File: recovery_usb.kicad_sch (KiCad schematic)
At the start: 19 parts, among them J3 USB-C_WE_632723300011, U56 HD3SS3220IRNHR, U57 TPD4E05U06QDQARQ1, U58 TPD4E05U06QDQARQ1, U59 TPD4E05U06QDQARQ1

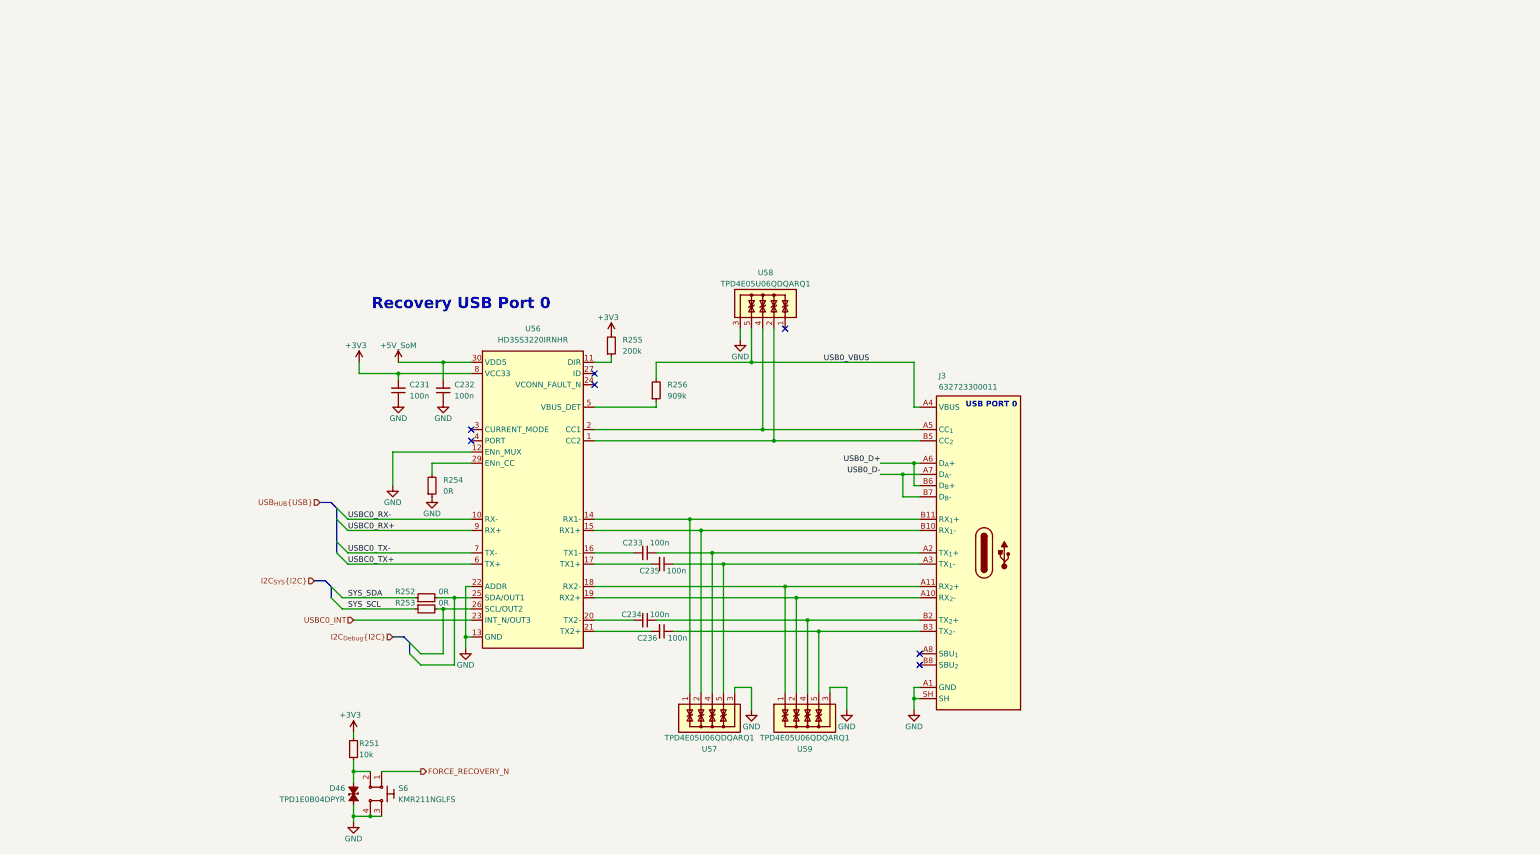
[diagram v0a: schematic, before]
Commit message: [#82837] Fix USB recovery and flashing section
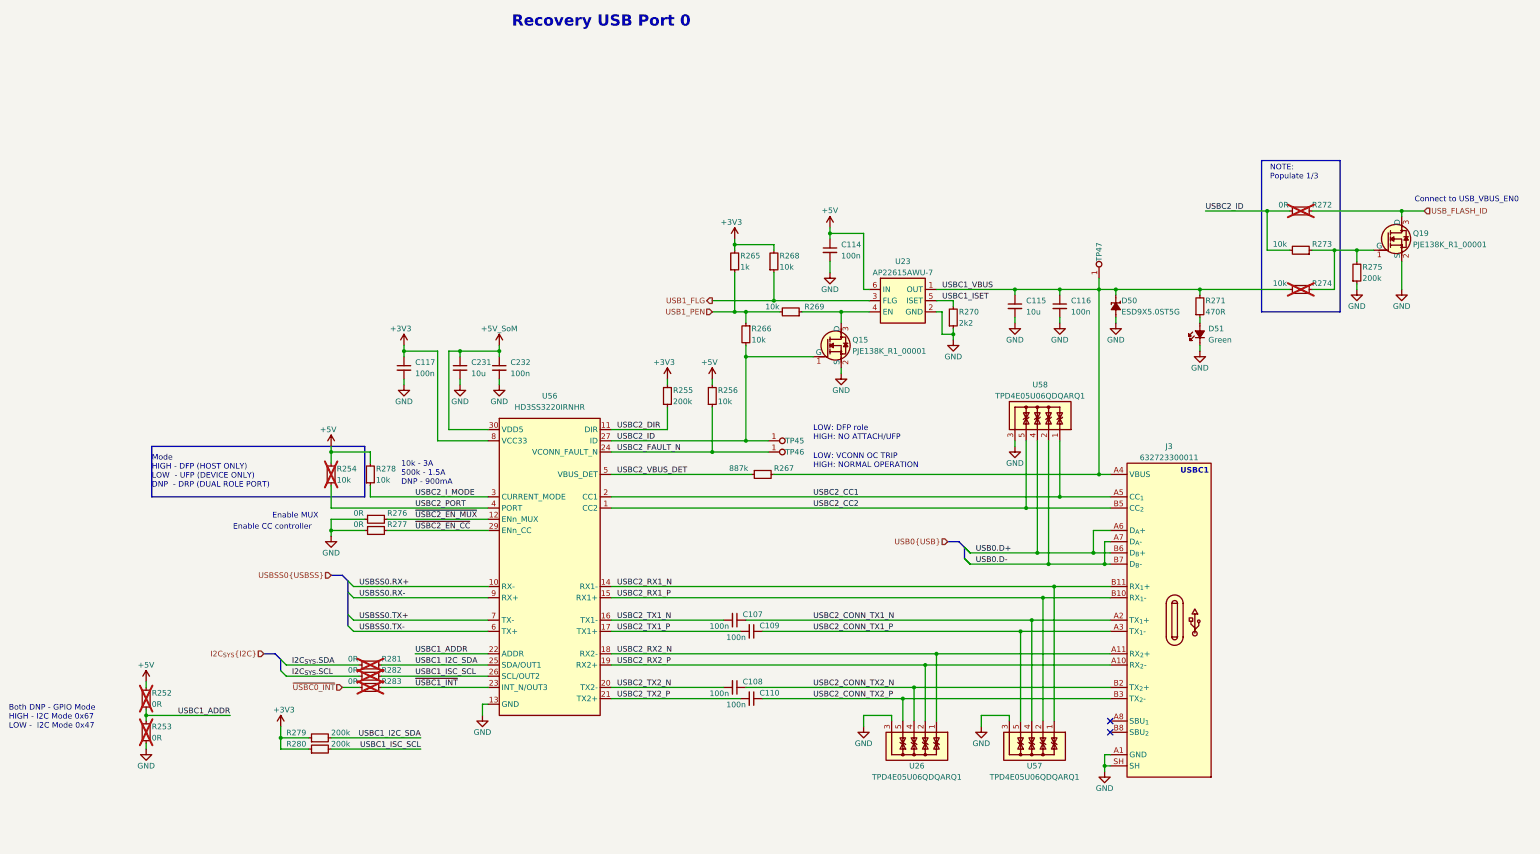
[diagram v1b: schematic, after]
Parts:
- removed C231, C232: C_100n_50V_X8L_0402, antmicro-footprints:C_0402_1005Metric, symbol antmicroCapacitors0402:C_100n_50V_X8L_0402
- removed C233, C234, C235, C236: C_100n_0201, antmicro-footprints:C_0201, symbol antmicroCapacitorsmisc:C_100n_0201
- removed D46: TPD1E0B04_XDFN-2, antmicro-footprints:XDFN-2_1x0.60mm, symbol antmicroTVSDiodes:TPD1E0B04_XDFN-2
- removed R251: R_10k_0402, antmicro-footprints:R_0402_1005Metric, symbol antmicroResistors0402:R_10k_0402
- removed R254: R_0R_0402, antmicro-footprints:R_0402_1005Metric, symbol antmicroResistors0402:R_0R_0402
- removed R256: R_909k_0402, antmicro-footprints:R_0402_1005Metric, symbol antmicroResistors0402:R_909k_0402
- removed S6: SW_KMR211NGLFS_SMD, antmicro-footprints:SW_KMR211NGLFS_SMD, symbol antmicroPushbuttonSwitches:SW_KMR211NGLFS_SMD
- removed U59: TPD4E05U06QDQARQ1, antmicro-footprints:USON-10_2.5x1mm_P0.5mm, symbol antmicroTVSDiodes:TPD4E05U06QDQARQ1
- added C107, C108, C109, C110, C114, C116, C117, C232: C_100n_0402, antmicro-footprints:C_0402_1005Metric, symbol antmicroCapacitors0402:C_100n_0402
- added C115, C231: C_10u_0603, antmicro-footprints:C_0603_1608Metric, symbol antmicroCapacitors0603:C_10u_0603
- added D50: ESD9X5.0ST5G, antmicro-footprints:SOD-923, symbol antmicroTVSDiodes:ESD9X5.0ST5G
- added D51: LED_G_0603_LTST-C190GKT, antmicro-footprints:LED_0603_1608Metric_G, symbol antmicroLEDIndicationDiscrete:LED_G_0603_LTST-C190GKT
- added Q15, Q19: PJE138K, antmicro-footprints:SOT-523, symbol antmicroTransistorsFETsMOSFETsSingle:PJE138K
- added R254, R256, R266, R268, R269, R273, R274, R278: R_10k_0402, antmicro-footprints:R_0402_1005Metric, symbol antmicroResistors0402:R_10k_0402
- added R265: R_1k_0402, antmicro-footprints:R_0402_1005Metric, symbol antmicroResistors0402:R_1k_0402
- added R267: R_887k_0402, antmicro-footprints:R_0402_1005Metric, symbol antmicroResistors0402:R_887k_0402
- added R270: R_2k2_0402, antmicro-footprints:R_0402_1005Metric, symbol antmicroResistors0402:R_2k2_0402
- added R271: R_470R_0402, antmicro-footprints:R_0402_1005Metric, symbol antmicroResistors0402:R_470R_0402
- added R272, R276, R277, R281, R282, R283: R_0R_0402, antmicro-footprints:R_0402_1005Metric, symbol antmicroResistors0402:R_0R_0402
- added R275, R279, R280: R_200k_0402, antmicro-footprints:R_0402_1005Metric, symbol antmicroResistors0402:R_200k_0402
- added TP45, TP46, TP47: TP_0.75mm_SMD, antmicro-footprints:TP_SMD_0.75mm, symbol antmicroTestPoints:TP_0.75mm_SMD
- added U23: AP22615A_TSOT26, antmicro-footprints:TSOT23-6, symbol antmicroPMICPowerDistributionSwitchesLoadDrivers:AP22615A_TSOT26
- added U26: TPD4E05U06QDQARQ1, antmicro-footprints:USON-10_2.5x1mm_P0.5mm, symbol antmicroTVSDiodes:TPD4E05U06QDQARQ1
- R252, R253: now not fitted; now left out of the parts list
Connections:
- net SYS_SCL is gone; now on net GND: R253.1
- net SYS_SDA is gone; now on net USBC1_ADDR: R252.1
- net USB0_D+ is gone; now on net USB0.D+: J3.A6 (D_{A}+), J3.B6 (D_{B}+)
- net USB0_D- is gone; now on net USB0.D-: J3.A7 (D_{A}-), J3.B7 (D_{B}-)
- net +3V3: now also C117.1, R265.2, R268.2, R279.1, R280.1
- net +5V_SoM: now also C231.1, C232.1
- net GND: now also C114.2, C115.2, C116.2, C117.2, C231.2, C232.2, D50.2 (A), D51.1 (C), Q15.2 (S), Q19.2 (S), R270.1, R275.1, R276.1, R277.1, U23.2 (GND), U26.3, U26.8; no longer U56.12 (ENn_MUX), U56.22 (ADDR)
- net USBC2_CONN_TX1_P: now reaches J3.A3 (TX_{1}-), U57.5, U57.6
- net USBC2_CONN_TX1_P: now also C109.1
- net USBC2_TX1_P: now reaches U56.17 (TX1+)
- net USBC2_TX1_P: now also C109.2
- net USB0.D-: now reaches U58.2, U58.9
- net USB0.D-: no longer J3.B5 (CC_{2}), U56.1 (CC2)
- net USBC2_DIR: now reaches R255.1, U56.11 (DIR)
- net USBC2_RX1_N: now reaches J3.B11 (RX_{1}+), U56.14 (RX1-), U57.1, U57.10
- net USBC2_RX1_P: now reaches J3.B10 (RX_{1}-), U56.15 (RX1+), U57.2, U57.9
- net USBC2_TX1_N: now reaches U56.16 (TX1-)
- net USBC2_TX1_N: now also C107.2
- net USBC2_RX2_N: now reaches J3.A11 (RX_{2}+), U56.18 (RX2-)
- net USBC2_RX2_N: now also U26.1, U26.10
- net USBC2_RX2_P: now reaches J3.A10 (RX_{2}-), U56.19 (RX2+)
- net USBC2_RX2_P: now also U26.2, U26.9
- net USB0.D+: now reaches U58.4, U58.7
- net USB0.D+: no longer J3.A5 (CC_{1}), U56.2 (CC1)
- net USBC2_TX2_N: now reaches U56.20 (TX2-)
- net USBC2_TX2_N: now also C108.2
- net USBC2_TX2_P: now reaches U56.21 (TX2+)
- net USBC2_TX2_P: now also C110.2
- net USBC2_FAULT_N: now reaches U56.24 (VCONN_FAULT_N)
- net USBC2_FAULT_N: now also R256.1, TP46.1
- net +5V: now reaches R252.2
- net +5V: now also C114.1, R254.1, R256.2, R278.2, U23.6 (IN); no longer U56.25 (SDA/OUT1)
- net USBC1_ADDR: now reaches R253.2
- net USBC1_ADDR: now also U56.22 (ADDR); no longer U56.26 (SCL/OUT2)
- net USBC2_ID: now reaches U56.27 (ID)
- net USBC2_ID: now also Q15.1 (G), R266.2, R272.1, R273.2, TP45.1
- net ~{USBC2_EN_CC}: now reaches U56.29 (ENn_CC)
- net ~{USBC2_EN_CC}: now also R277.2
- net USBC2_I_MODE: now reaches U56.3 (CURRENT_MODE)
- net USBC2_I_MODE: now also R278.1
- net USBC2_PORT: now reaches U56.4 (PORT)
- net USBC2_PORT: now also R254.2
- net USBC2_VBUS_DET: now reaches U56.5 (VBUS_DET)
- net USBC2_VBUS_DET: now also R267.1
- net USBC2_CONN_TX2_P: now reaches J3.B3 (TX_{2}-)
- net USBC2_CONN_TX2_P: now also C110.1, U26.5, U26.6
- net USBC2_CONN_TX1_N: now reaches J3.A2 (TX_{1}+), U57.4, U57.7
- net USBC2_CONN_TX1_N: now also C107.1
- net USBC2_CONN_TX2_N: now reaches J3.B2 (TX_{2}+)
- net USBC2_CONN_TX2_N: now also C108.1, U26.4, U26.7
- net USBC2_CC1: now reaches U58.1, U58.10
- net USBC2_CC1: now also J3.A5 (CC_{1}), U56.2 (CC1)
- net USB0_VBUS renamed USBC1_VBUS
- net USBC1_VBUS: now also C115.1, C116.1, D50.1 (C), R267.2, R271.2, R274.2, TP47.1, U23.1 (OUT); no longer U58.5, U58.6
- net USBC0_INT renamed ~{USBC1_INT}
- net ~{USBC1_INT}: now also R283.2
- net USBC0_RX+ renamed USBSS0.RX-
- net USBC0_RX- renamed USBSS0.RX+
- net USBC0_TX+ renamed USBSS0.TX-
- net USBC0_TX- renamed USBSS0.TX+
- new net: Q15.3 (D), R269.1, U23.4 (EN)
- new net: Q19.1 (G), R273.1, R274.1, R275.2
- new net: D51.2 (A), R271.1
- new net I2C_{SYS}.SCL: R282.1
- new net I2C_{SYS}.SDA: R281.1
- new net USB1_FLG: R268.1, U23.3 (FLG)
- new net USB1_PEN: R265.1, R266.1, R269.2
- new net USBC1_I2C_SDA: R279.2, R281.2, U56.25 (SDA/OUT1)
- new net USBC1_ISC_SCL: R280.2, R282.2, U56.26 (SCL/OUT2)
- new net USBC1_ISET: R270.2, U23.5 (ISET)
- new net USBC2_CC2: J3.B5 (CC_{2}), U56.1 (CC2), U58.5, U58.6
- new net USB_FLASH_ID: Q19.3 (D), R272.2
- new net ~{USBC0_INT}: R283.1
- new net ~{USBC2_EN_MUX}: R276.2, U56.12 (ENn_MUX)
- no-connect marks 7 -> 2
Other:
- note added: "10k - 3A 500k - 1.5A DNP - 900mA"
- note added: "Both DNP - GPIO Mode HIGH - I2C Mode 0x67 LOW - I2C Mode 0x47"
- note added: "Connect to USB_VBUS_EN0"
- note added: "Enable CC controller"
- note added: "Enable MUX"
- note added: "LOW: DFP role HIGH: NO ATTACH/UFP"
- note added: "LOW: VCONN OC TRIP HIGH: NORMAL OPERATION"
- note added: "Mode HIGH - DFP (HOST ONLY) LOW - UFP (DEVICE ONLY) DNP - DRP (DUAL ROLE PORT)"
- note added: "NOTE: Populate 1/3"
- note added: "USBC1"
- note removed: "USB PORT 0"
- moved on the sheet: U56

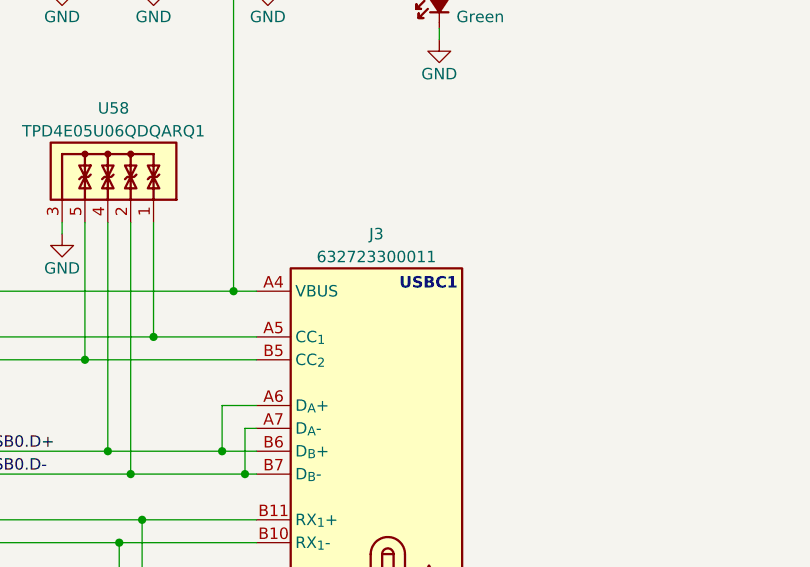
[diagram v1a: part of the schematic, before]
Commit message: [#82837] Finish rerouting USB PD controller, start debug section
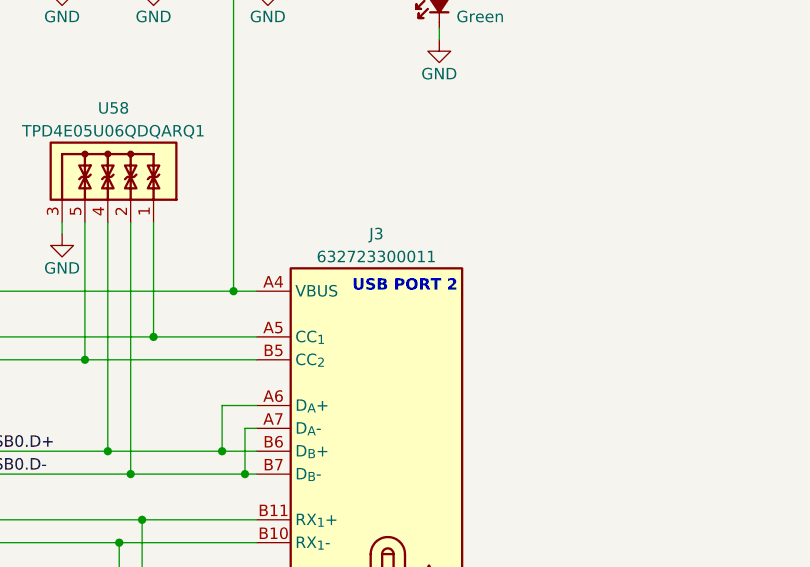
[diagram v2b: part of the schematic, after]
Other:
- note added: "USB PORT 2"
- note removed: "USBC1"
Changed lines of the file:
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@@
-		)
-	)
-	(text "USBC1"
-		(exclude_from_sim no)
-		(at 316.865 127 0)
-		(effects
-			(font
-				(size 1.27 1.27)
-				(thickness 0.254)
-				(bold yes)
-			)
-			(justify left bottom)
 		)
 	)
@@
 		)
 	)
+	(text "USB PORT 2"
+		(exclude_from_sim no)
+		(at 317.5 126.492 0)
+		(effects
+			(font
+				(size 1.27 1.27)
+				(thickness 0.254)
+				(bold yes)
+			)
+		)
+	)

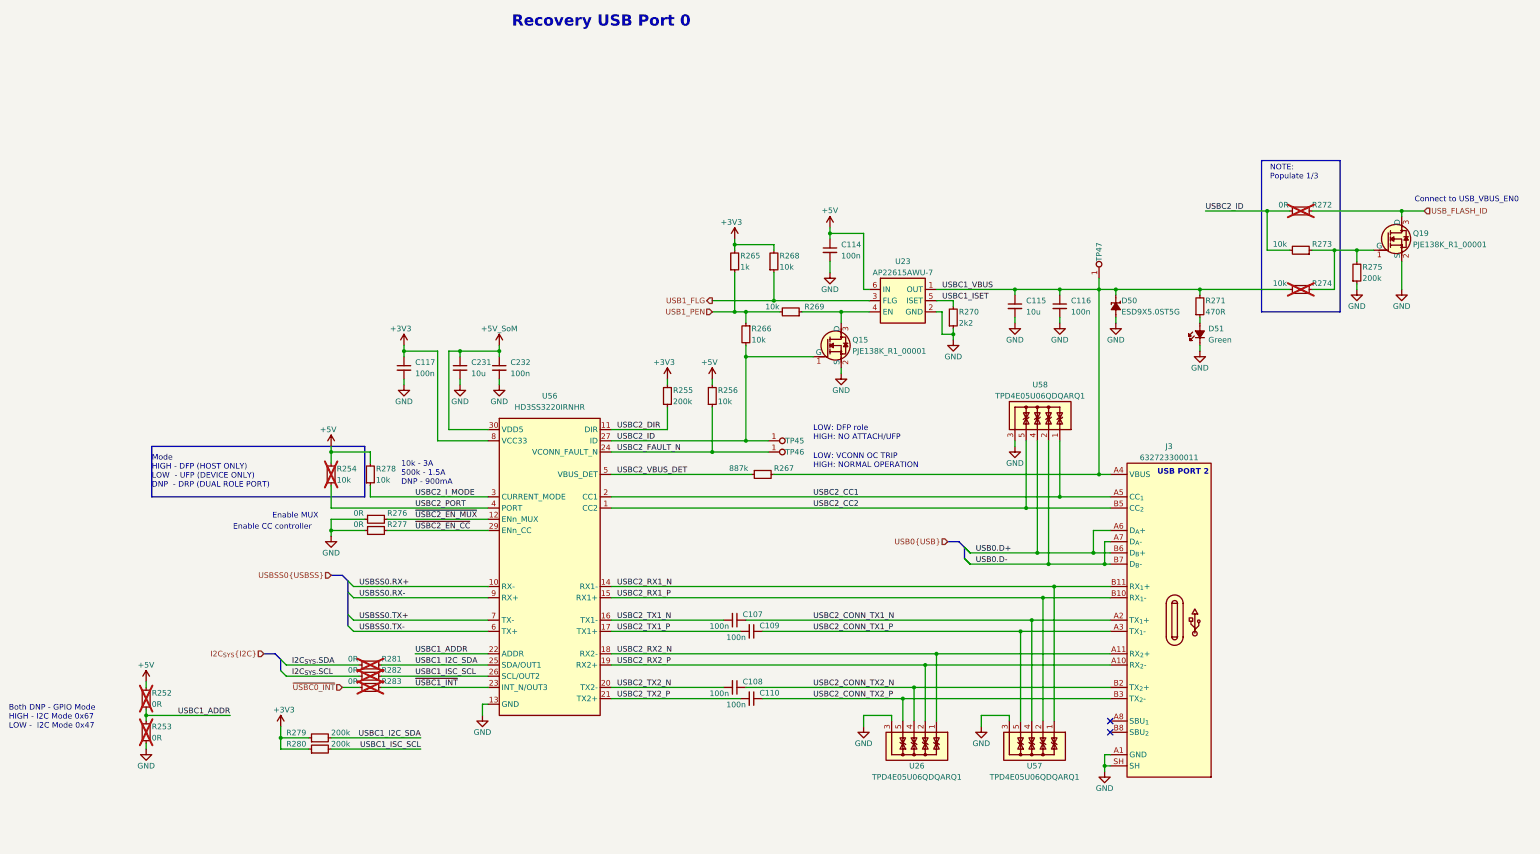
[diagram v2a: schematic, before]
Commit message: [#82837] Finish mapping interfaces, waiting for new SoM symbol
[#82837] Add GPIO level shifter and route USB related GPIO on root
schematic

[#82837] WIP: Modify Power-up and reset section
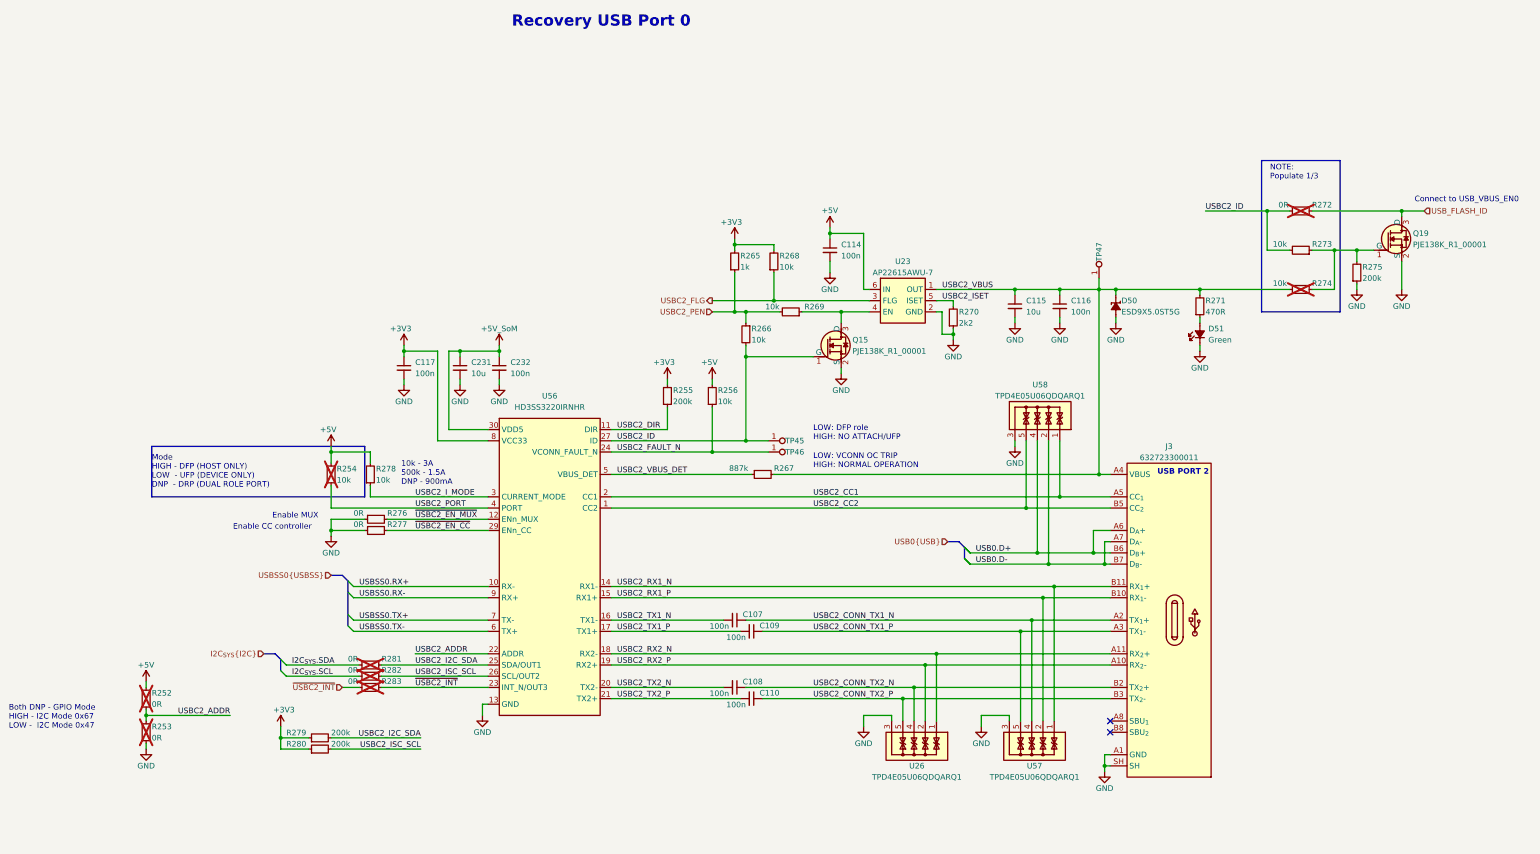
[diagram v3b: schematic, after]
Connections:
- net ~{USBC1_INT} is gone; now on net ~{USBC2_INT}: R283.2, U56.23 (INT_N/OUT3)
- net USB1_FLG renamed USBC2_FLG
- net USB1_PEN renamed USBC2_PEN
- net USBC1_ADDR renamed USBC2_ADDR
- net USBC1_I2C_SDA renamed USBC2_I2C_SDA
- net USBC1_ISC_SCL renamed USBC2_ISC_SCL
- net USBC1_ISET renamed USBC2_ISET
- net USBC1_VBUS renamed USBC2_VBUS
- net ~{USBC0_INT} renamed ~{USBC2_INT}
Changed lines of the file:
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@@
 		)
 	)
-	(label "USBC1_ADDR"
+	(label "USBC2_ADDR"
 		(at 143.51 167.64 0)
 		(effects
@@
 		)
 	)
-	(label "USBC1_I2C_SDA"
+	(label "USBC2_I2C_SDA"
 		(at 143.51 170.18 0)
 		(effects
@@
 		)
 	)
-	(label "USBC1_ISC_SCL"
+	(label "USBC2_ISC_SCL"
 		(at 144.78 189.23 180)
 		(effects
@@
 		)
 	)
-	(label "~{USBC1_INT}"
+	(label "~{USBC2_INT}"
 		(at 143.51 175.26 0)
 		(effects
@@
 		)
 	)
-	(label "USBC1_ADDR"
+	(label "USBC2_ADDR"
 		(at 101.6 181.61 180)
 		(effects
@@
 		)
 	)
-	(label "USBC1_I2C_SDA"
+	(label "USBC2_I2C_SDA"
 		(at 144.78 186.69 180)
 		(effects
@@
 		)
 	)
-	(label "USBC1_ISC_SCL"
+	(label "USBC2_ISC_SCL"
 		(at 143.51 172.72 0)
 		(effects
@@
 		)
 	)
-	(label "USBC1_VBUS"
+	(label "USBC2_VBUS"
 		(at 262.89 85.09 0)
 		(effects
@@
 		)
 	)
-	(label "USBC1_ISET"
+	(label "USBC2_ISET"
 		(at 262.89 87.63 0)
 		(effects
@@
 		)
 	)
-	(hierarchical_label "USB1_FLG"
+	(hierarchical_label "USBC2_FLG"
 		(shape output)
 		(at 210.82 87.63 180)
@@
 		)
 	)
-	(hierarchical_label "USB1_PEN"
+	(hierarchical_label "USBC2_PEN"
 		(shape input)
 		(at 210.82 90.17 180)
@@
 		)
 	)
-	(hierarchical_label "~{USBC0_INT}"
+	(hierarchical_label "~{USBC2_INT}"
 		(shape input)
 		(at 127 175.26 180)
